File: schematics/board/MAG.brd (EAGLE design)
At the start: 22 x 22 mm, 12 parts

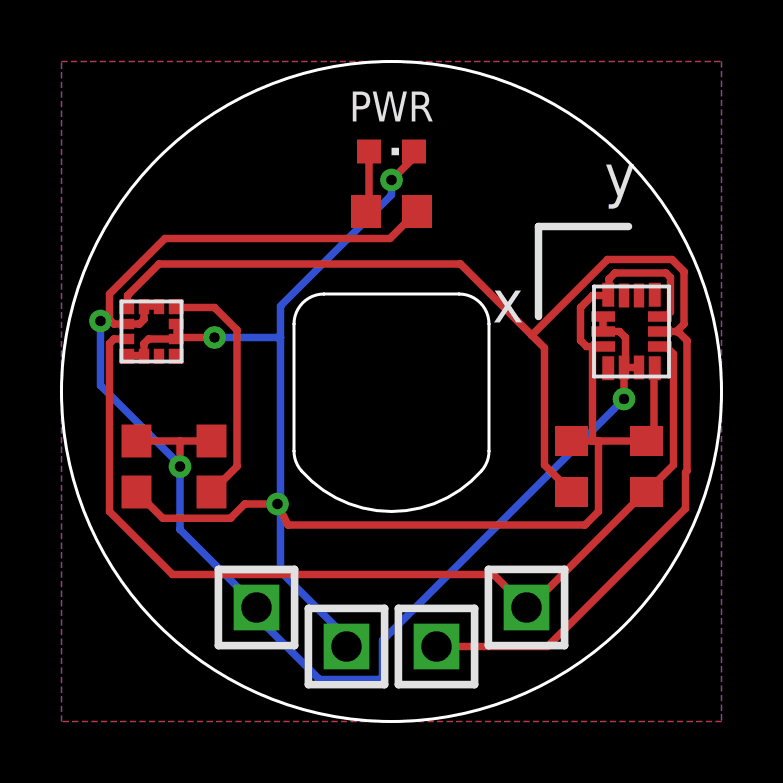
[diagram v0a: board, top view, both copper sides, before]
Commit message: Исправлены MAG и BSK1
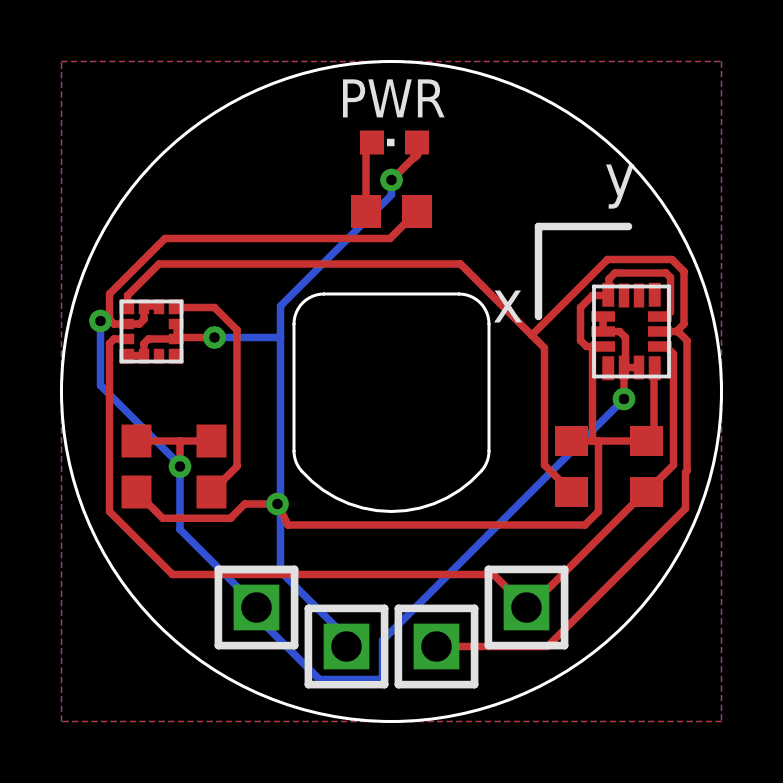
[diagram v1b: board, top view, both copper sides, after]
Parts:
- moved PWR 0.32 mm to (11.1, 19.3), turned to 90 degrees
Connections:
- net N$1: now also PWR.C; no longer PWR.A
- net VDD: now also PWR.A; no longer PWR.C
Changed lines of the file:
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@@
 <attribute name="VALUE" x="11.23" y="-0.675" size="1.27" layer="27"/>
-</element>
-<element name="PWR" library="led" library_urn="urn:adsk.eagle:library:259" package="CHIPLED_0603" package3d_urn="urn:adsk.eagle:package:15822/2" value="" x="11" y="19" smashed="yes" rot="R270">
-<attribute name="NAME" x="11" y="20" size="1" layer="25" align="bottom-center"/>
-<attribute name="POPULARITY" value="28" x="8.46" y="5.03" size="1.778" layer="27" rot="R270" display="off"/>
-<attribute name="VALUE" x="9.73" y="17.095" size="1.27" layer="27"/>
 </element>
 <element name="LIS3MDL" library="CanCubeSat" package="LIS3MDL" value="LIS3MDL" x="3" y="13" smashed="yes" rot="R90"/>
@@
 <element name="R101" library="resistor" library_urn="urn:adsk.eagle:library:348" package="R0603" package3d_urn="urn:adsk.eagle:package:23555/3" value="5k1" x="17" y="8.5" smashed="yes" rot="R270"/>
 <element name="R102" library="resistor" library_urn="urn:adsk.eagle:library:348" package="R0603" package3d_urn="urn:adsk.eagle:package:23555/3" value="5k1" x="19.5" y="8.5" smashed="yes" rot="R270"/>
+<element name="PWR" library="led" library_urn="urn:adsk.eagle:library:259" package="CHIPLED_0603" package3d_urn="urn:adsk.eagle:package:15822/2" value="" x="11.1" y="19.3" smashed="yes" rot="R90">
+<attribute name="NAME" x="9.23" y="20.135" size="1.27" layer="25"/>
+<attribute name="POPULARITY" value="28" x="5.8" y="14.4" size="1.778" layer="27" rot="R90" display="off"/>
+<attribute name="VALUE" x="12.37" y="21.205" size="1.27" layer="27" rot="R180"/>
+</element>
 </elements>
 <signals>
-<signal name="N$1">
-<contactref element="R1" pad="2"/>
-<contactref element="PWR" pad="A"/>
-<wire x1="10.25" y1="17.1" x2="10.25" y2="19" width="0.25" layer="1"/>
-<wire x1="10.15" y1="17" x2="10.25" y2="17.1" width="0.25" layer="1"/>
-</signal>
 <signal name="VDD">
-<contactref element="PWR" pad="C"/>
 <contactref element="LIS3MDL" pad="P$6"/>
 <contactref element="LIS3MDL" pad="P$5"/>
@@
 <wire x1="2.75" y1="12.6" x2="2.9" y2="12.75" width="0.25" layer="1"/>
 <wire x1="2.75" y1="12.175" x2="2.75" y2="12.6" width="0.25" layer="1"/>
-<wire x1="11.75" y1="18.8" x2="11.75" y2="19" width="0.25" layer="1"/>
 <wire x1="11" y1="18.05" x2="11.75" y2="18.8" width="0.25" layer="1"/>
 <wire x1="11" y1="17.55" x2="11" y2="18.05" width="0.25" layer="16"/>
@@
 <wire x1="3.375" y1="6.775" x2="2.5" y2="7.65" width="0.25" layer="1"/>
 <wire x1="18.05" y1="12.5" x2="17.5" y2="12.5" width="0.25" layer="1"/>
+<contactref element="PWR" pad="A"/>
+<wire x1="11.75" y1="18.8" x2="11.85" y2="18.9" width="0.3" layer="1"/>
+<wire x1="11.85" y1="18.9" x2="11.85" y2="19.3" width="0.3" layer="1"/>
+<wire x1="17.7" y1="12.4" x2="17.5" y2="12.5" width="0" layer="19" extent="1-1"/>
 </signal>
 <signal name="GND">
@@
 <wire x1="3.85" y1="13.8" x2="3.825" y2="13.825" width="0.25" layer="1"/>
 </signal>
+<signal name="N$1">
+<contactref element="PWR" pad="C"/>
+<contactref element="R1" pad="2"/>
+<wire x1="10.15" y1="17" x2="10.15" y2="19.1" width="0.25" layer="1"/>
+<wire x1="10.15" y1="19.1" x2="10.35" y2="19.3" width="0.25" layer="1"/>
+</signal>
 </signals>

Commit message: Обновлены герберы плат
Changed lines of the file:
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@@
 <layers>
 <layer number="1" name="Top" color="4" fill="1" visible="yes" active="yes"/>
+<layer number="2" name="Route2" color="16" fill="1" visible="no" active="yes"/>
+<layer number="3" name="Route3" color="17" fill="1" visible="no" active="yes"/>
+<layer number="4" name="Route4" color="18" fill="1" visible="no" active="yes"/>
+<layer number="5" name="Route5" color="19" fill="1" visible="no" active="yes"/>
+<layer number="6" name="Route6" color="25" fill="1" visible="no" active="yes"/>
+<layer number="7" name="Route7" color="26" fill="1" visible="no" active="yes"/>
+<layer number="8" name="Route8" color="27" fill="1" visible="no" active="yes"/>
+<layer number="9" name="Route9" color="28" fill="1" visible="no" active="yes"/>
+<layer number="10" name="Route10" color="29" fill="1" visible="no" active="yes"/>
+<layer number="11" name="Route11" color="30" fill="1" visible="no" active="yes"/>
+<layer number="12" name="Route12" color="20" fill="1" visible="no" active="yes"/>
+<layer number="13" name="Route13" color="21" fill="1" visible="no" active="yes"/>
+<layer number="14" name="Route14" color="22" fill="1" visible="no" active="yes"/>
+<layer number="15" name="Route15" color="23" fill="1" visible="no" active="yes"/>
 <layer number="16" name="Bottom" color="1" fill="1" visible="yes" active="yes"/>
 <layer number="17" name="Pads" color="2" fill="1" visible="yes" active="yes"/>
@@
 <layer number="24" name="bOrigins" color="15" fill="1" visible="no" active="yes"/>
 <layer number="25" name="tNames" color="7" fill="1" visible="yes" active="yes"/>
-<layer number="26" name="bNames" color="7" fill="1" visible="no" active="yes"/>
+<layer number="26" name="bNames" color="7" fill="1" visible="yes" active="yes"/>
 <layer number="27" name="tValues" color="7" fill="1" visible="no" active="yes"/>
 <layer number="28" name="bValues" color="7" fill="1" visible="no" active="yes"/>
-<layer number="29" name="tStop" color="7" fill="3" visible="no" active="yes"/>
-<layer number="30" name="bStop" color="7" fill="6" visible="no" active="yes"/>
+<layer number="29" name="tStop" color="7" fill="3" visible="yes" active="yes"/>
+<layer number="30" name="bStop" color="7" fill="6" visible="yes" active="yes"/>
 <layer number="31" name="tCream" color="7" fill="4" visible="no" active="yes"/>
 <layer number="32" name="bCream" color="7" fill="5" visible="no" active="yes"/>
@@
 <circle x="11" y="11" radius="4" width="0.25" layer="41"/>
 <wire x1="15.9" y1="16.5" x2="18.9" y2="16.5" width="0.25" layer="21"/>
-<wire x1="18.9" y1="16.5" x2="17.8" y2="16.8" width="0.25" layer="22"/>
-<wire x1="18.9" y1="16.5" x2="17.8" y2="16.2" width="0.25" layer="22"/>
+<wire x1="18.9" y1="16.5" x2="17.8" y2="16.8" width="0.25" layer="21"/>
+<wire x1="18.9" y1="16.5" x2="17.8" y2="16.2" width="0.25" layer="21"/>
 <wire x1="15.9" y1="16.5" x2="15.9" y2="13.5" width="0.25" layer="21"/>
-<wire x1="15.9" y1="13.5" x2="16.2" y2="14.6" width="0.25" layer="22"/>
-<wire x1="15.9" y1="13.5" x2="15.6" y2="14.6" width="0.25" layer="22"/>
+<wire x1="15.9" y1="13.5" x2="16.2" y2="14.6" width="0.25" layer="21"/>
+<wire x1="15.9" y1="13.5" x2="15.6" y2="14.6" width="0.25" layer="21"/>
 <text x="15.4" y="13.3" size="1.4224" layer="25" font="vector" rot="MR0">x</text>
 <text x="18.1" y="17.5" size="1.4224" layer="25" font="vector">y</text>
@@
 <param name="mvStopFrame" value="1"/>
 <param name="mvCreamFrame" value="0"/>
-<param name="mlMinStopFrame" value="4mil"/>
-<param name="mlMaxStopFrame" value="4mil"/>
+<param name="mlMinStopFrame" value="1mil"/>
+<param name="mlMaxStopFrame" value="1mil"/>
 <param name="mlMinCreamFrame" value="0mil"/>
 <param name="mlMaxCreamFrame" value="0mil"/>
@@
 <wire x1="11.75" y1="18.8" x2="11.85" y2="18.9" width="0.3" layer="1"/>
 <wire x1="11.85" y1="18.9" x2="11.85" y2="19.3" width="0.3" layer="1"/>
-<wire x1="17.7" y1="12.4" x2="17.5" y2="12.5" width="0" layer="19" extent="1-1"/>
 </signal>
 <signal name="GND">

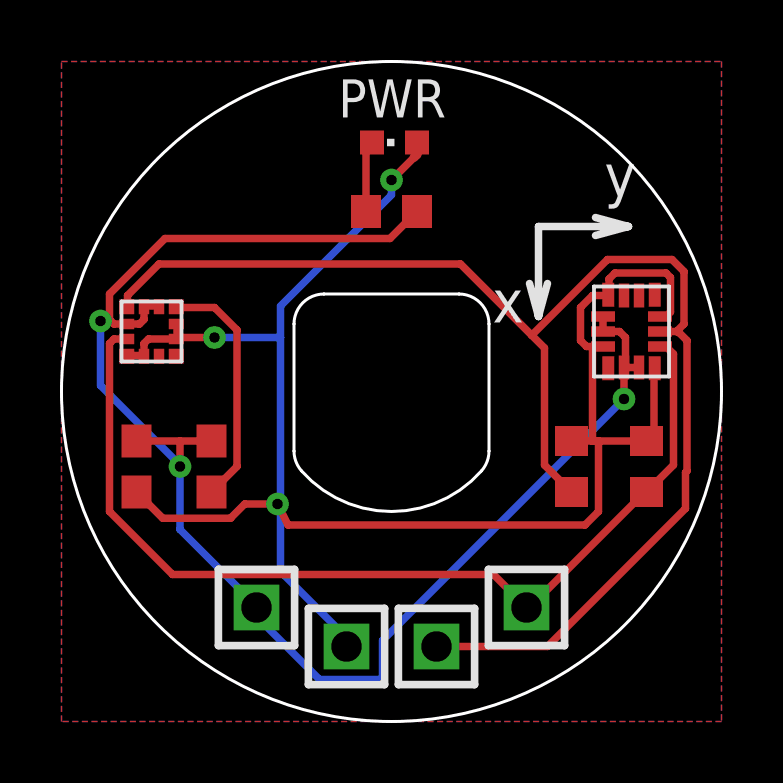
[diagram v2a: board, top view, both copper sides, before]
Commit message: Исправлена плата MAG
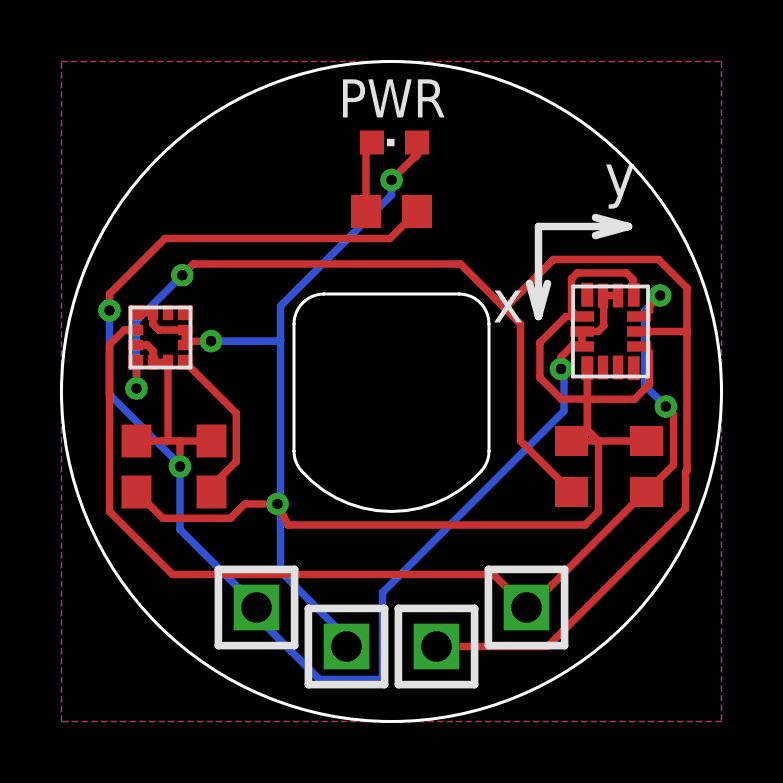
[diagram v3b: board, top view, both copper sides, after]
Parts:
- moved LSM6DS3 0.70 mm to (18.3, 13.0)
- moved LIS3MDL 0.36 mm to (3.30, 12.8)
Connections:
- net GND: now also LIS3MDL.P$12, LIS3MDL.P$2, LIS3MDL.P$3, LSM6DS3.P$2, LSM6DS3.P$3, LSM6DS3.P$7; no longer LIS3MDL.P$11, LIS3MDL.P$8, LIS3MDL.P$9, LSM6DS3.P$10, LSM6DS3.P$5, LSM6DS3.P$9
- net N$3: now also LIS3MDL.P$4; no longer LIS3MDL.P$7
- net SCL: now also LIS3MDL.P$1; no longer LIS3MDL.P$10
- net SDA: now also LIS3MDL.P$11, LSM6DS3.P$14; no longer LIS3MDL.P$12, LSM6DS3.P$12
- net VDD: now also LIS3MDL.P$10, LIS3MDL.P$9, LSM6DS3.P$1, LSM6DS3.P$12, LSM6DS3.P$5, LSM6DS3.P$8; no longer LIS3MDL.P$1, LIS3MDL.P$2, LSM6DS3.P$11, LSM6DS3.P$14, LSM6DS3.P$4, LSM6DS3.P$7
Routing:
- net SCL: track 46.3 -> 50.2 mm, vias 0 -> 2
- net SDA: track 32.6 -> 36.1 mm, vias 0 -> 2
- net N$3: track 8.10 -> 5.37 mm
- net VDD: track 60.2 -> 62.4 mm
- net GND: track 51.8 -> 53.7 mm
